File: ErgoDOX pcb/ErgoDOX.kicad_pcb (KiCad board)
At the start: 2 copper layers, 182.8 x 158.9 mm, 77 parts, among them J1 USB, J2 3.5mm, J3 JMP, J4 JMP, SW0:10 SW0:3, SW0:11 SW0:2, SW0:12 SW0:1, SW0:7 SW0:6, SW0:8 SW0:5, SW0:9 SW0:4, SW1:10 SW1:3, SW1:11 SW1:2, SW1:12 SW1:1, SW1:13 SW1:0, SW1:9 SW1:4, SW2:10 SW2:3, SW2:11 SW2:2, SW2:12 SW2:1, SW2:13 SW2:0, SW2:7 SW2:6, SW2:8 SW2:5, SW2:9 SW2:4, SW3:10 SW3:3, SW3:11 SW3:2, SW3:12 SW3:1, SW3:13 SW3:0, SW3:8 SW3:5, SW3:9 SW3:4, SW4:10 SW4:3, SW4:11 SW4:2, SW4:12 SW4:1, SW4:13 SW4:0, SW4:7 SW4:6, SW4:8 SW4:5, SW4:9 SW4:4, SW5:10 SW5:3, SW5:11 SW5:2, SW5:12 SW5:1, SW5:13 SW5:0, SW5:7 SW5:6, SW5:8 SW5:5, SW5:9 SW5:4, U1 TEENSY2.0, U2 MCP23018

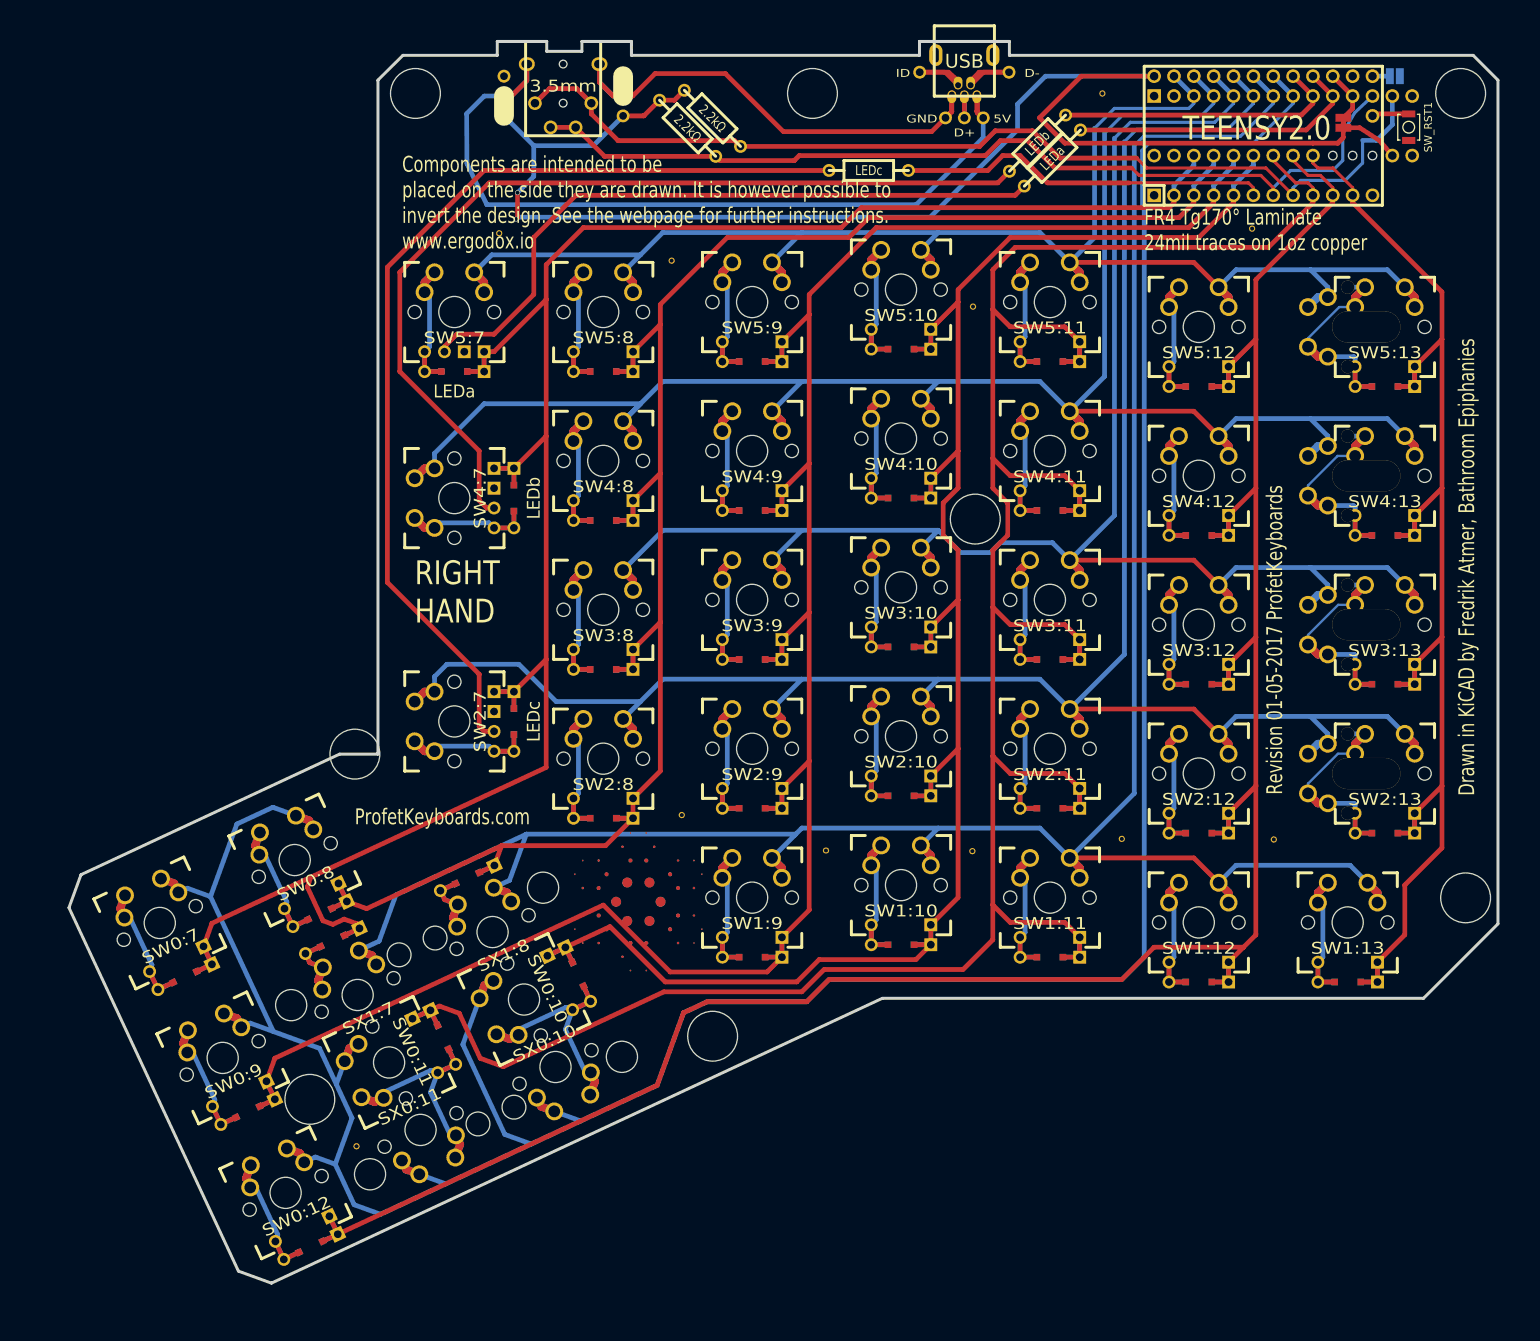
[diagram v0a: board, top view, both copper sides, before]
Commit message: Replaced teensy with atmega
Imported project into new version of KiCad
Initial routing of traces is done
Switch footprints need some investigation - overlap is throwing design rule errors
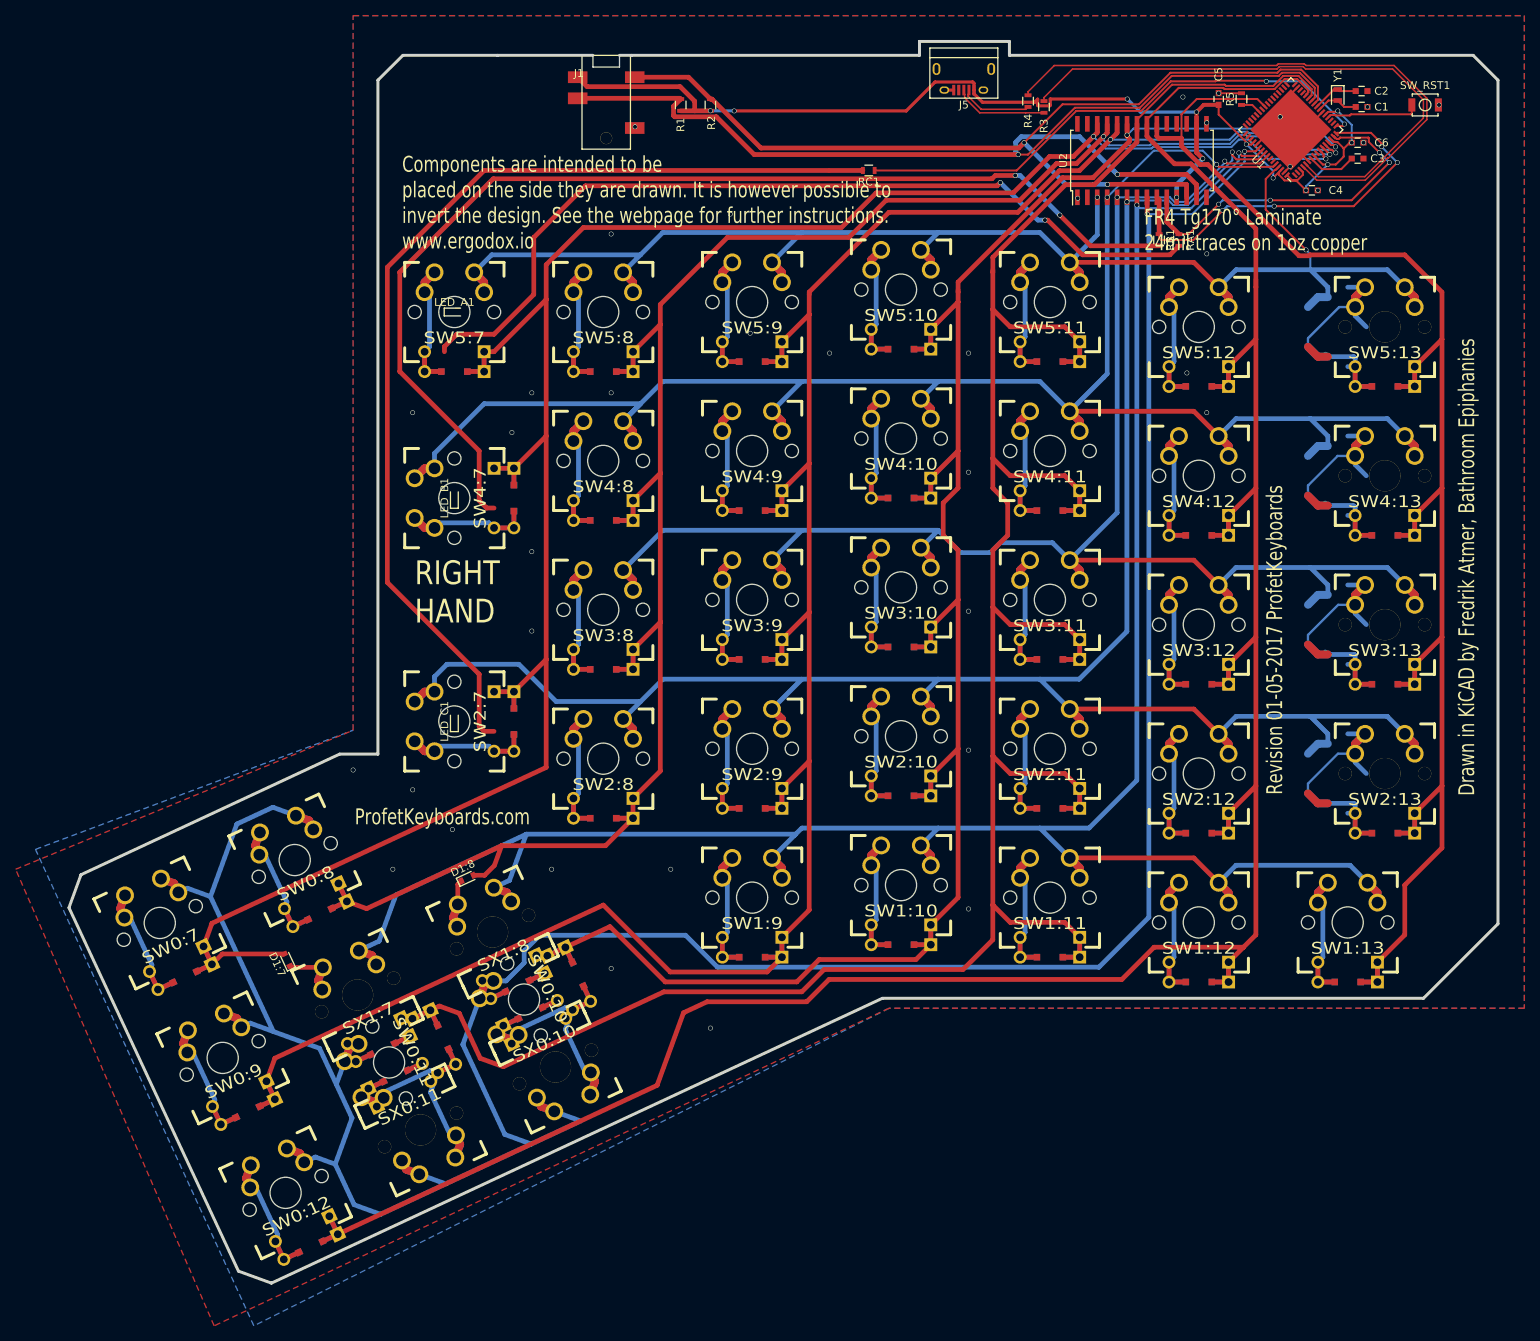
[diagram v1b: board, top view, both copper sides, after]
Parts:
- removed H99: MECHANICAL, ErgoDOXmech
- removed J2: 3.5mm, 4pin35mmAudio
- removed J3, J4: JMP, 100PITCH1X3
- removed JP1, JP2: JUMPER, GAP
- removed S1, S2: STAB200, STAB_PCB940
- removed STAR_1: STAR_FRONT, ErgoDOX pcb:STAR
- removed STAR_2: STAR_BACK, ErgoDOX pcb:STAR
- removed STITCHING_VIA (x11): ~, lib_footprints:STITCHING_VIA
- added C1: 10p, Capacitors_SMD:C_0603, F.Cu at (188.5, 38.9)
- added C2: 10p, Capacitors_SMD:C_0603, F.Cu at (188.5, 36.8)
- added C3: 1u, Capacitors_SMD:C_0603, F.Cu at (188.0, 45.5)
- added C4: 1u, Capacitors_SMD:C_0603, F.Cu at (182.1, 49.5)
- added C5: 100n, Capacitors_SMD:C_0603, F.Cu at (170.2, 37.8)
- added C6: 100n, Capacitors_SMD:C_0603, F.Cu at (188.0, 43.4)
- added J5: USB_B_Micro, Connectors:USB_Micro-B, F.Cu at (137.6, 35.4)
- added R3: 22, Resistors_SMD:R_0603, F.Cu at (147.8, 38.9)
- added R4: 22, Resistors_SMD:R_0603, F.Cu at (145.8, 38.1)
- added R5: 1k, Resistors_SMD:R_0603, F.Cu at (173.1, 37.9)
- added Y1: 16MHz, Crystals:Crystal_SMD_2012-2pin_2.0x1.2mm, F.Cu at (185.4, 37.3)
- D1:7, D1:8: footprint DIODE -> Diodes_SMD:D_0603
- J1: value USB -> AudioJack4; footprint USBMINImod -> ErgoDOX pcb:ASJ-112-M
- LED_A1, LED_B1, LED_C1: footprint MX_LED -> LEDs:LED_0603
- R1, R2, RA1, RB1, RC1: footprint RESISTOR -> Resistors_SMD:R_0603
- SW2:13, SW3:13, SW4:13, SW5:13: footprint ErgoDOX pcb:MX_FLIP_XX -> ErgoDOX pcb:MX_FLIP_DIODE
- SX0:10, SX0:11, SX1:7, SX1:8: footprint MX_FLIP -> ErgoDOX pcb:MX_FLIP_DIODE
- U1: value TEENSY2.0 -> AT90USB1286-MU; footprint ErgoDOX pcb:TEENSY_2.0_WITH_RESET -> Housings_DFN_QFN:QFN-64-1EP_9x9mm_Pitch0.5mm
- U2: footprint DIP28_300 -> Housings_SOIC:SOIC-28W_7.5x17.9mm_Pitch1.27mm; moved to F.Cu
- moved J1 45.9 mm to (91.8, 32.3), turned to 0 degrees
- moved RB1 19.9 mm to (162.6, 55.9), turned to 270 degrees
- moved RA1 19.3 mm to (165.1, 55.9), turned to 270 degrees
- moved U2 18.6 mm to (160.4, 45.7), turned to 90 degrees
- moved D1:7 6.28 mm to (51.0, 148.0), turned to 115 degrees
- moved R1 4.41 mm to (101.3, 38.6), turned to 90 degrees
- moved R2 4.18 mm to (105.2, 38.6), turned to 90 degrees
- moved U1 3.61 mm to (179.4, 41.8), turned to 135 degrees
- moved SW_RST1 3.53 mm to (196.6, 38.6), turned to 0 degrees
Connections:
- U1 pad 1: GND -> (no net)
- U1 pad 10: /COL1 -> /COL6
- U1 pad 11: /COL0 -> /COL5
- U1 pad 12: Net-(U1-Pad12) -> /COL4
- U1 pad 16: /RST -> /LED_B
- U1 pad 18: GND -> (no net)
- U1 pad 19: Net-(U1-Pad19) -> (no net)
- U1 pad 2: /COL6 -> (no net)
- U1 pad 20: VCC -> /RST
- U1 pad 21: /LED_A -> VCC
- U1 pad 22: /LED_B -> GND
- U1 pad 23: /ROW0 -> Net-(C1-Pad2)
- U1 pad 24: /ROW1 -> Net-(C2-Pad1)
- U1 pad 25: /ROW2 -> /SCLM
- U1 pad 26: /ROW3 -> /SDAM
- U1 pad 27: /ROW4 -> /COL11
- U1 pad 28: /ROW5 -> /COL1
- U1 pad 29: VCC -> (no net)
- U1 pad 3: /COL5 -> VCC
- U1 pad 4: /COL4 -> /D-
- U1 pad 5: /COL10 -> /D+
- U1 pad 6: /LED_C -> GND
- U1 pad 7: /SCLM -> Net-(C3-Pad1)
- U1 pad 8: /SDAM -> VCC
- U1 pad 9: /COL11 -> (no net)
- U2 pad 14: Net-(U2-Pad14) -> (no net)
- U2 pad 17: Net-(U2-Pad17) -> (no net)
- U2 pad 18: Net-(U2-Pad18) -> (no net)
- U2 pad 19: Net-(U2-Pad19) -> (no net)
- U2 pad 27: Net-(U2-Pad27) -> (no net)
- U2 pad 28: Net-(U2-Pad28) -> (no net)
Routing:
- net Net-(J1-Pad1): track 102.6 -> 0.00 mm
- net /D-: track 0.00 -> 77.3 mm
- net /D+: track 0.00 -> 73.6 mm
- net Net-(J1-Pad5): track 62.3 -> 0.00 mm
- net VCC: track 204.8 -> 148.3 mm, vias 2 -> 12
- net /COL0: track 159.7 -> 196.3 mm
- net /COL1: track 291.8 -> 321.6 mm
- net Net-(LED_A1-Pad1): track 87.6 -> 111.9 mm, vias 0 -> 2
- net Net-(LED_B1-Pad1): track 119.1 -> 141.7 mm, vias 0 -> 2
- net /COL5: track 225.8 -> 248.3 mm, vias 0 -> 2
- net /LED_C: track 47.6 -> 68.3 mm, vias 0 -> 2
- net /COL6: track 259.5 -> 278.2 mm, vias 0 -> 2
- net /COL4: track 274.3 -> 292.1 mm, vias 0 -> 2
- net /COL10: track 233.7 -> 249.0 mm, vias 0 -> 2
- net /LED_B: track 36.8 -> 49.7 mm, vias 0 -> 4
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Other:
- outline, holes or cut-outs redrawn
- net class Default: clearance 0.3048 -> 0.1524; trace_width 0.6 -> 0.6096
- rule pad_to_mask_clearance: 0.2032 -> 0.0508
- rule trace_clearance: 0.3048 -> 0.1524
- board text removed: "5V"
- board text removed: "D+"
- board text removed: "D-"
- board text removed: "GND"
- board text removed: "ID"

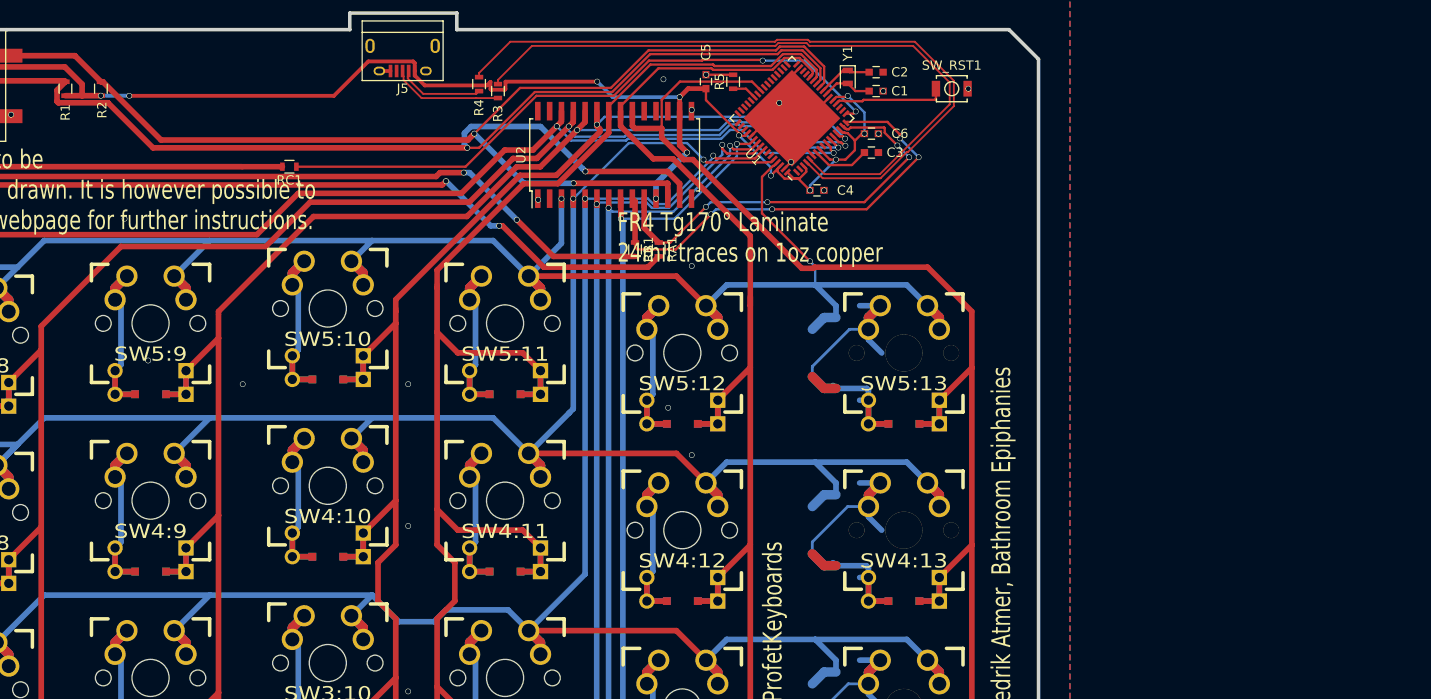
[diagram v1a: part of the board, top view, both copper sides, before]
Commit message: migrated to newer KiCAD
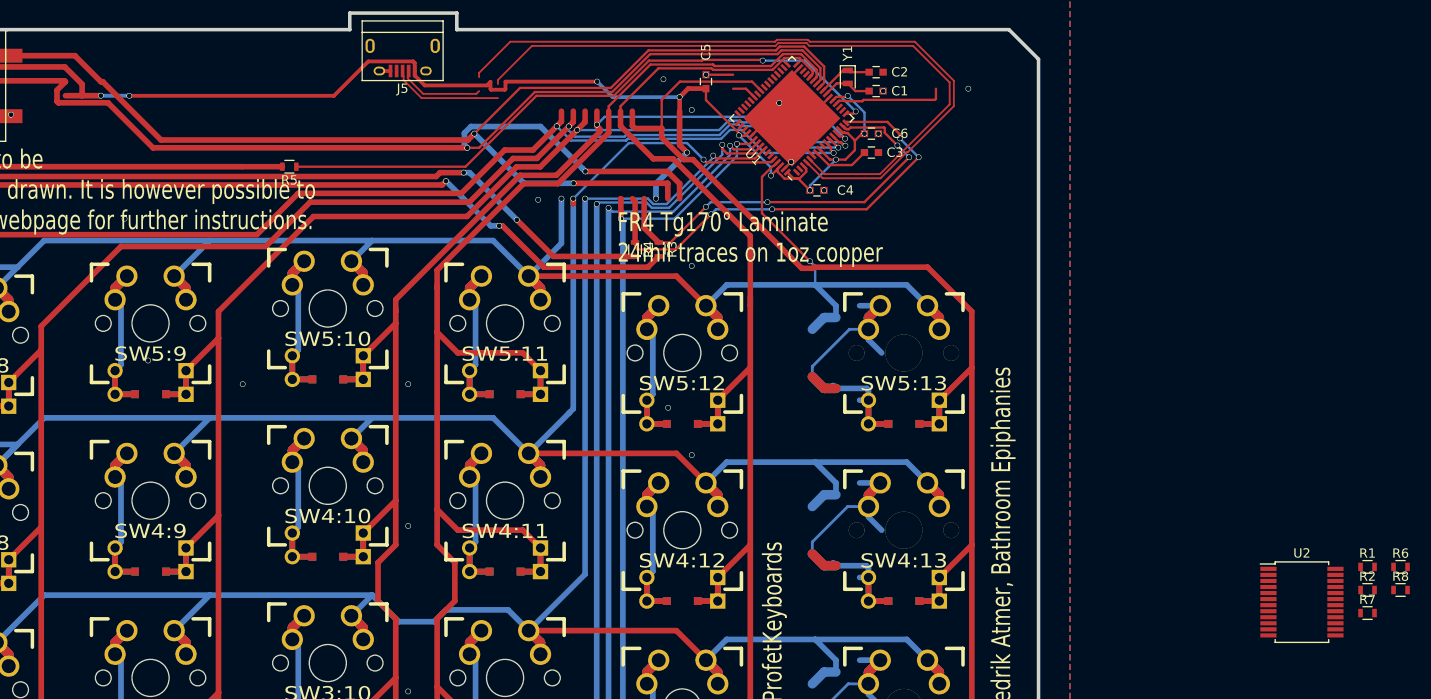
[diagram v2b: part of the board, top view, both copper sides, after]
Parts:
- removed the R3 at (147.8, 38.9)
- removed the R4 at (145.8, 38.1)
- removed the R5 at (173.1, 37.9)
- removed SW_RST1: SWITCH_PUSH, Buttons_Switches_SMD:SW_SPST_B3U-1000P
- added R6: 1k, Resistors_SMD:R_0603, F.Cu at (244.8, 90.0)
- added R7: 1k, Resistors_SMD:R_0603, F.Cu at (241.3, 95.0)
- added R8: 1k, Resistors_SMD:R_0603, F.Cu at (244.8, 92.5)
- LED_A1: value LEDa -> LED
- LED_B1: value LEDb -> LED
- LED_C1: value LEDc -> LED
- R1, R2: value 2.2kΩ -> 22
- R3: renamed from RA1; value LEDa -> 1k
- R4: renamed from RB1; value LEDb -> 1k
- R5: renamed from RC1; value LEDc -> 1k
- U2: footprint Housings_SOIC:SOIC-28W_7.5x17.9mm_Pitch1.27mm -> Housings_SSOP:SSOP-24_5.3x8.2mm_Pitch0.65mm
- moved R1 149.1 mm to (241.3, 90.0), turned to 0 degrees
- moved R2 146.4 mm to (241.3, 92.5), turned to 0 degrees
- moved U2 88.1 mm to (234.2, 93.8), turned to 0 degrees
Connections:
- C4 pad 2: GND -> Net-(C4-Pad2)
- C5 pad 2: GND -> Net-(C4-Pad2)
- C6 pad 2: GND -> Net-(C4-Pad2)
- D1:7 pad 1: Net-(D1:7-Pad1) -> /COL6
- D1:7 pad 2: /COL6 -> Net-(D1:7-Pad2)
- D1:8 pad 1: Net-(D1:8-Pad1) -> /COL5
- D1:8 pad 2: /COL5 -> Net-(D1:8-Pad2)
- LED_A1 pad 1: Net-(LED_A1-Pad1) -> GND
- LED_A1 pad 2: GND -> Net-(LED_A1-Pad2)
- LED_B1 pad 1: Net-(LED_B1-Pad1) -> GND
- LED_B1 pad 2: GND -> Net-(LED_B1-Pad2)
- LED_C1 pad 1: Net-(LED_C1-Pad1) -> GND
- LED_C1 pad 2: GND -> Net-(LED_C1-Pad2)
- R1 pad 1: VCC -> /D+
- R1 pad 2: /SDAM -> /d+
- R2 pad 1: VCC -> /D-
- R2 pad 2: /SCLM -> /d-
- R3 pad 2: Net-(LED_A1-Pad1) -> Net-(LED_A1-Pad2)
- R4 pad 2: Net-(LED_B1-Pad1) -> Net-(LED_B1-Pad2)
- R5 pad 2: Net-(LED_C1-Pad1) -> Net-(LED_C1-Pad2)
- SW0:10 pad 3: Net-(SW0:10-Pad2) -> Net-(SW0:10-Pad3)
- SW0:10 pad 4: /COL10 -> Net-(SW0:10-Pad4)
- SW0:11 pad 3: Net-(SW0:11-Pad2) -> Net-(SW0:11-Pad3)
- SW0:11 pad 4: /COL11 -> Net-(SW0:11-Pad4)
- SW0:12 pad 4: /COL1 -> Net-(SW0:12-Pad4)
- SW0:7 pad 4: /COL6 -> Net-(SW0:7-Pad4)
- SW0:8 pad 4: /COL5 -> Net-(SW0:8-Pad4)
- SW0:9 pad 4: /COL4 -> Net-(SW0:9-Pad4)
- SW1:10 pad 4: /COL10 -> Net-(SW1:10-Pad4)
- SW1:11 pad 4: /COL11 -> Net-(SW1:11-Pad4)
- SW1:12 pad 4: /COL1 -> Net-(SW1:12-Pad4)
- SW1:13 pad 4: /COL0 -> Net-(SW1:13-Pad4)
- SW1:9 pad 4: /COL4 -> Net-(SW1:9-Pad4)
- SW2:10 pad 4: /COL10 -> Net-(SW2:10-Pad4)
- SW2:11 pad 4: /COL11 -> Net-(SW2:11-Pad4)
- SW2:12 pad 4: /COL1 -> Net-(SW2:12-Pad4)
- SW2:13 pad 4: /COL0 -> Net-(SW2:13-Pad4)
- SW2:7 pad 4: /COL6 -> Net-(SW2:7-Pad4)
- SW2:8 pad 4: /COL5 -> Net-(SW2:8-Pad4)
- SW2:9 pad 4: /COL4 -> Net-(SW2:9-Pad4)
- SW3:10 pad 4: /COL10 -> Net-(SW3:10-Pad4)
- SW3:11 pad 4: /COL11 -> Net-(SW3:11-Pad4)
- SW3:12 pad 4: /COL1 -> Net-(SW3:12-Pad4)
- SW3:13 pad 4: /COL0 -> Net-(SW3:13-Pad4)
- SW3:8 pad 4: /COL5 -> Net-(SW3:8-Pad4)
- SW3:9 pad 4: /COL4 -> Net-(SW3:9-Pad4)
- SW4:10 pad 4: /COL10 -> Net-(SW4:10-Pad4)
- SW4:11 pad 4: /COL11 -> Net-(SW4:11-Pad4)
- SW4:12 pad 4: /COL1 -> Net-(SW4:12-Pad4)
- SW4:13 pad 4: /COL0 -> Net-(SW4:13-Pad4)
- SW4:7 pad 4: /COL6 -> Net-(SW4:7-Pad4)
- SW4:8 pad 4: /COL5 -> Net-(SW4:8-Pad4)
- SW4:9 pad 4: /COL4 -> Net-(SW4:9-Pad4)
- SX0:10 pad 1: /ROW0 -> Net-(SX0:10-Pad1)
- SX0:10 pad 2: Net-(SW0:10-Pad2) -> Net-(SW0:10-Pad3)
- SX0:11 pad 1: /ROW0 -> Net-(SX0:11-Pad1)
- SX0:11 pad 2: Net-(SW0:11-Pad2) -> Net-(SW0:11-Pad3)
- SX1:7 pad 2: Net-(D1:7-Pad1) -> Net-(D1:7-Pad2)
- SX1:8 pad 2: Net-(D1:8-Pad1) -> Net-(D1:8-Pad2)
- U1 pad 20: /RST -> (no net)
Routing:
- net Net-(LED_B1-Pad2): track 0.00 -> 141.7 mm, vias 0 -> 2
- net Net-(LED_B1-Pad1): track 141.7 -> 0.00 mm, vias 2 -> 0
- net Net-(LED_C1-Pad2): track 0.00 -> 131.7 mm
- net Net-(LED_C1-Pad1): track 131.7 -> 0.00 mm
- net Net-(LED_A1-Pad2): track 0.00 -> 111.9 mm, vias 0 -> 2
- net Net-(LED_A1-Pad1): track 111.9 -> 0.00 mm, vias 2 -> 0
- net /RST: track 12.1 -> 0.00 mm
- net (no net): track 0.00 -> 12.1 mm
- net Net-(D1:7-Pad2): track 0.00 -> 8.85 mm
- net /COL6: track 278.2 -> 269.3 mm
- net Net-(C4-Pad2): track 0.00 -> 2.93 mm, vias 0 -> 3
- net GND: track 13.6 -> 10.7 mm, vias 37 -> 34
